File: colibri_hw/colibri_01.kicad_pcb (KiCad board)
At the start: 2 copper layers, 79.9 x 64 mm, 33 parts, among them J1 XT30UPB-M, J2 Conn_01x03_Male, J3 Conn_01x03_Male, J4 Conn_01x03_Male, J5 Conn_01x03_Male, J6 Conn_01x05_Male, J7 Conn_01x05_Male, M4 MountingHole_4.3mm_M4_Pad_Via, SW1 SW_Push, U1 ESP-12E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

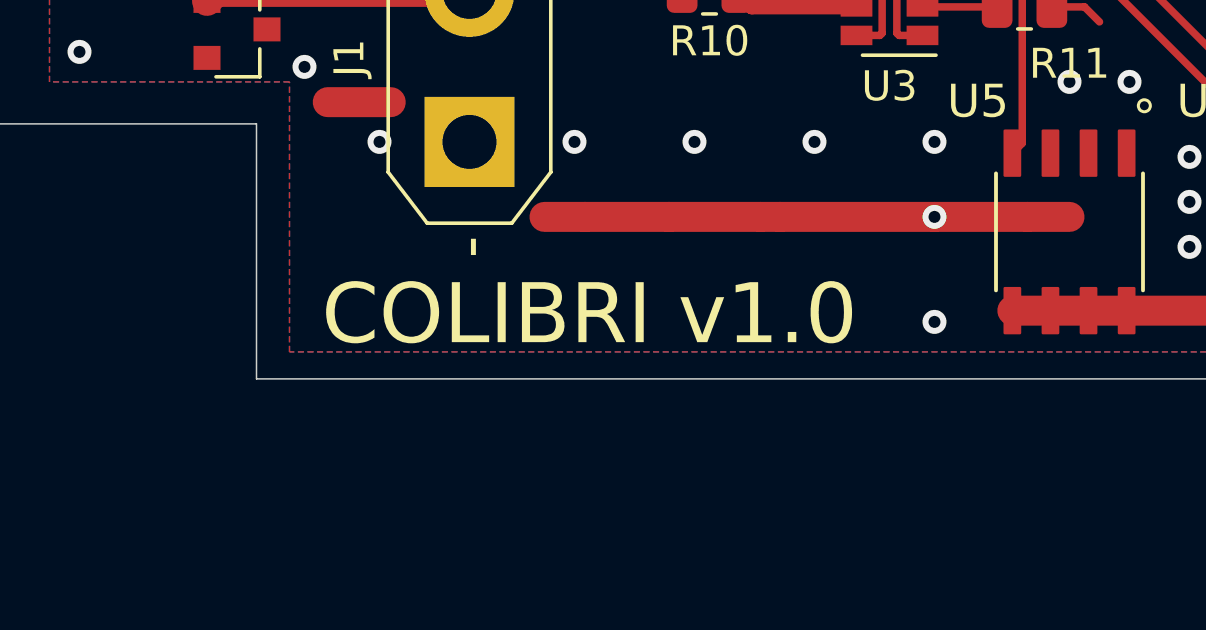
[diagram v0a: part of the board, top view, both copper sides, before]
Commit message: [v1.0.1]: Fix UART communication issues due to R5 value
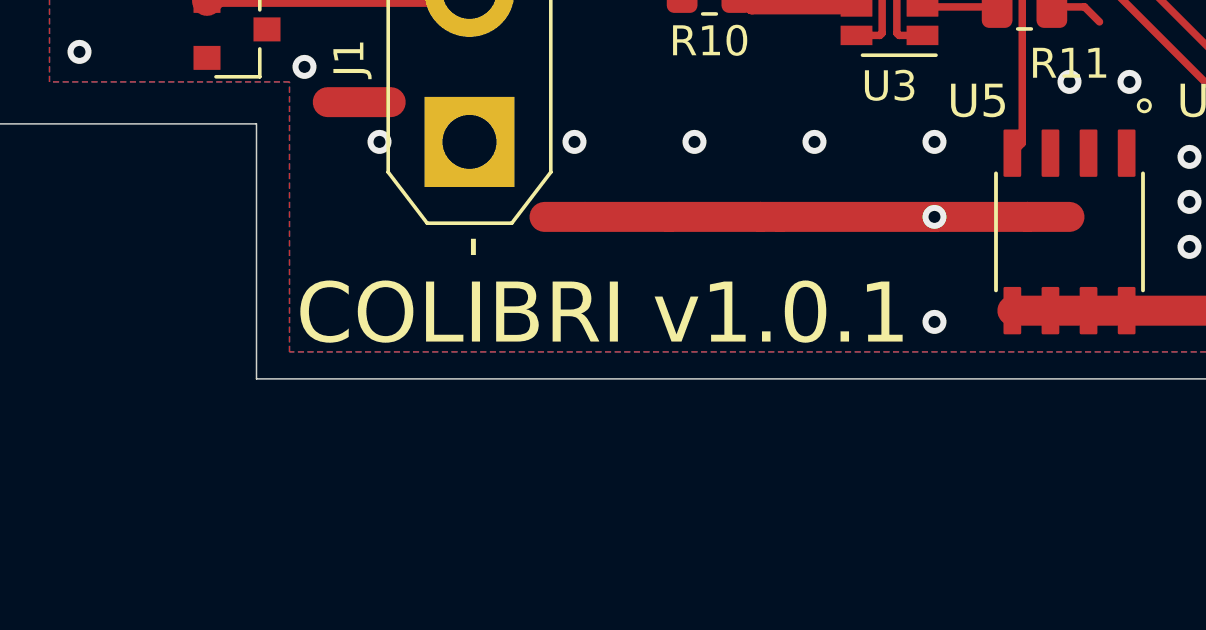
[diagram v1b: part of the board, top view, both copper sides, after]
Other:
- board text added: "COLIBRI v1.0.1"
- board text removed: "COLIBRI v1.0"
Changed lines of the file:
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@@
     (effects (font (size 1 1) (thickness 0.15)))
   )
-  (gr_text "COLIBRI v1.0" (at 130 119.25) (layer "F.SilkS")
+  (gr_text "COLIBRI v1.0.1" (at 130.45 119.23) (layer "F.SilkS")
     (effects (font (size 2 2) (thickness 0.15)))
   )
